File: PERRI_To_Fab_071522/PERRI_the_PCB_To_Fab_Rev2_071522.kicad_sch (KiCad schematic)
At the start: 40 parts, among them J1 SS5-80-3.00-X-D-K-XX, J2 Conn_01x02, J3 Conn_02x50_Counter_Clockwise, J4 Conn_02x05_Counter_Clockwise, J5 SS5-80-3.00-X-D-K-XX, J6 Conn_01x03, J7 Conn_01x03, J8 Conn_01x03, SW2 SW_DIP_x08, U1 TMP441AIDCNR, U2 TPS2595, U3 PCA9554ADB, U4 NCV8508

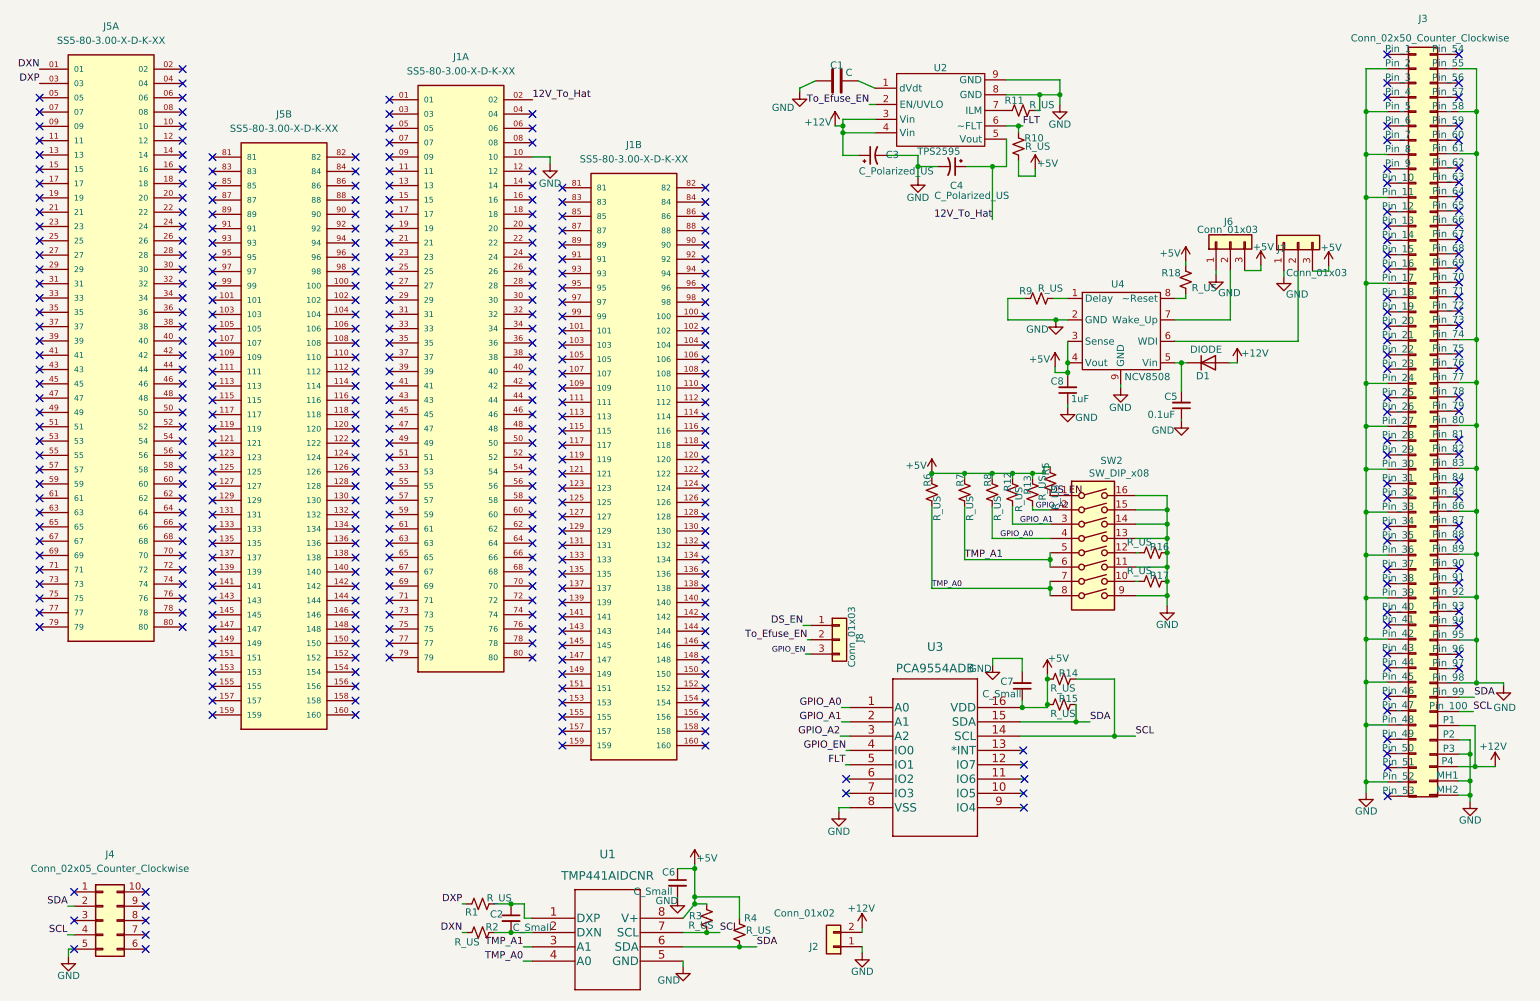
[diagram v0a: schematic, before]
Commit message: changed 2x5 connector on PERRI
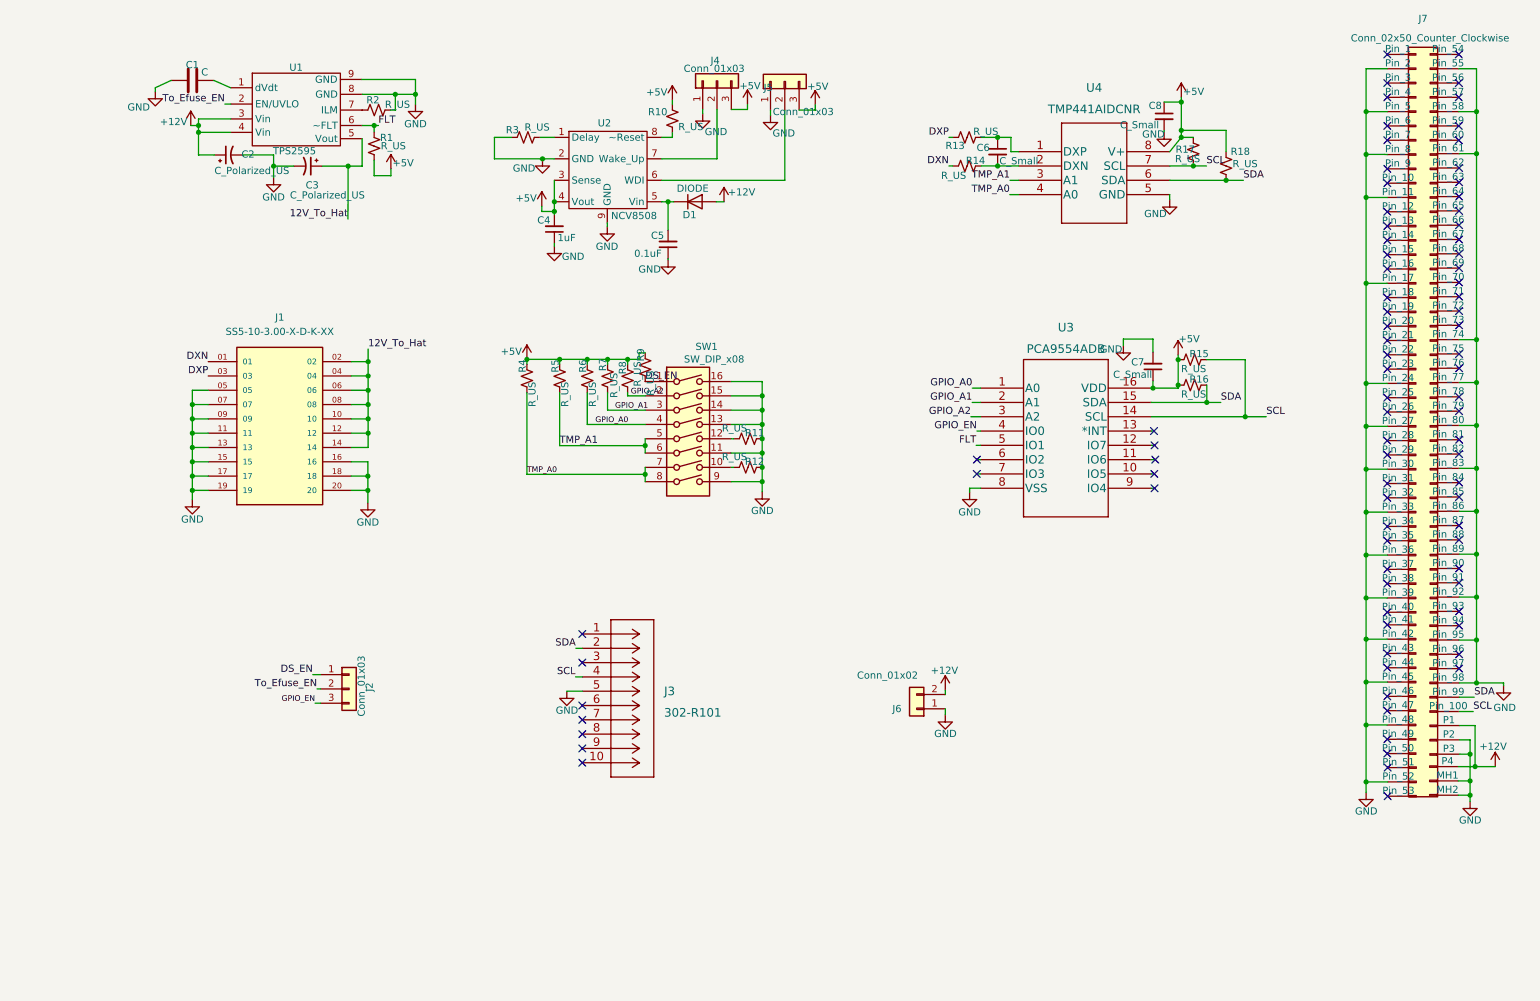
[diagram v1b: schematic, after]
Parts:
- removed J1, J5: SS5-80-3.00-X-D-K-XX, footprints:SAMTEC_SS5-80-3.00-X-D-K-XX, symbol SS5-80-3.00-X-D-K-XX:SS5-80-3.00-X-D-K-XX
- removed J4: Conn_02x05_Counter_Clockwise, footprints:302010030000, symbol Connector_Generic:Conn_02x05_Counter_Clockwise
- added J1: SS5-10-3.00-X-D-K-XX, footprints:SAMTEC_SS5-10-3.00-X-D-K-XX, symbol SS5-10-3.00-X-D-K-XX:SS5-10-3.00-X-D-K-XX
- added J3: 302-R101, footprints:302-R101, symbol 2022-07-15_19-29-03:302-R101
- renumbered C3 to C2, C4 to C3, C8 to C4, C2 to C6, C6 to C8, J8 to J2, J6 to J4, J7 to J5, J2 to J6, J3 to J7, R10 to R1, R18 to R10, R16 to R11, R17 to R12, R1 to R13, R2 to R14, R14 to R15, R15 to R16, R3 to R17, R4 to R18, R11 to R2, R9 to R3, R6 to R4, R7 to R5, R8 to R6, R12 to R7, R13 to R8, R5 to R9, SW2 to SW1, U2 to U1, U4 to U2, U1 to U4
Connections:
- net 12V_To_Hat: now also J1.02, J1.04, J1.06, J1.08, J1.10, J1.12, J1.14
- net DXN: now also J1.01
- net DXP: now also J1.03
- net GND: now also J1.05, J1.07, J1.09, J1.11, J1.13, J1.15, J1.16, J1.17, J1.18, J1.19, J1.20, J3.5
- net SCL: now also J3.4
- net SDA: now also J3.2
- no-connect marks 402 -> 85
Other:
- moved on the sheet: C1, C2, C3, C4, C5, C6, C7, C8, D1, J2, J4, J5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
